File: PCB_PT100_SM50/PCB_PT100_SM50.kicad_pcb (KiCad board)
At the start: 2 copper layers, 80 x 65 mm, 62 parts, among them U1 TPD4E1U06DBVR, U2 INA826AIDR, U3 TPS7A4901DGNT, U4 INA826AIDR, U5 OPA2188AIDR, U6 REF3012AIDBZR, U7 TPD4E1U06DBVR, U8 78L05 5V

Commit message: Publish final PCB project
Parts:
- added C24: 100nF, Capacitor_SMD:C_0805_2012Metric, F.Cu at (27.9, 41.2)
- added C25: 10uF, Capacitor_SMD:C_0805_2012Metric, F.Cu at (34.9, 41.1)
- added C26: 0.1uF, Capacitor_SMD:C_0805_2012Metric, F.Cu at (30.9, 42.1)
- added G***: LOGO, Images:logoucr, F.Cu at (64.3, 20.2)
- added REF**: KiCad-Logo2_5mm_SilkScreen, Symbol:KiCad-Logo2_5mm_SilkScreen, F.Cu at (81.9, 42.2)
- J_PT100_1: footprint TerminalBlock_Phoenix:TerminalBlock_Phoenix_MKDS-1,5-3_1x03_P5.00mm_Horizontal -> ProyectoPCB:CONN_AST0250304_MZC
- J_SM50: footprint TerminalBlock_Phoenix:TerminalBlock_Phoenix_MKDS-1,5-4_1x04_P5.00mm_Horizontal -> ProyectoPCB:AST0250404
- U3: footprint Package_SO:MSOP-8-1EP_3x3mm_P0.65mm_EP1.73x1.85mm -> ProyectoPCB_Footprints:TPS7A4901DGNT_DGN8_1P89X1P57
- moved C13 44.3 mm to (76.9, 71.1), turned to 0 degrees
- moved C17 41.7 mm to (56.9, 42.2), turned to -90 degrees
- moved C15 40.9 mm to (58.9, 42.0), turned to -90 degrees
- moved C16 40.8 mm to (62.9, 50.1)
- moved C11 40.7 mm to (76.9, 69.1), turned to 0 degrees
- moved C18 39.0 mm to (64.9, 50.0)
- moved U6 36.9 mm to (29.9, 46.1)
- moved F6 29.7 mm to (64.1, 45.2), turned to 180 degrees
- moved C22 29.4 mm to (25.9, 44.2), turned to 180 degrees
- moved C20 29.2 mm to (49.1, 63.2), turned to 0 degrees
- moved R2 28.4 mm to (30.8, 31.2)
- moved F4 26.4 mm to (71.1, 73.1), turned to 180 degrees
- moved F5 25.9 mm to (63.7, 40.2), turned to 180 degrees
- moved C10 24.0 mm to (52.0, 27.2), turned to 0 degrees
- moved C2 23.1 mm to (33.6, 30.2), turned to 90 degrees
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- renumbered C_OUT_SM50 to C27, C_OUT_PT100 to C28, R_LIM_SM50 to R11, R_ISO_PT100 to R12, R_ISO_SM50 to R13, RSET_PT100 to R14, R_LIM_PT100 to R9, TRIM_SM50 to RV1, TRIM_PT100 to RV2
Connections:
- H1 pad 1: (no net) -> GND
- H2 pad 2: (no net) -> GND
- H3 pad 3: (no net) -> GND
- H4 pad 4: (no net) -> GND
- J_BBOX_PT100 pad 3: Net-(J_BBOX_PT100-GND_3) -> GND
- J_BBOX_PT100 pad 6: Net-(J_BBOX_PT100-GND_3) -> GND
- J_BBOX_SM50 pad 3: Net-(J_BBOX_SM50-GND_3) -> GND
- J_BBOX_SM50 pad 6: Net-(J_BBOX_SM50-GND_3) -> GND
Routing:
- net /+15V_PROT_PT100: track 0.00 -> 81.3 mm
- net /+15V_PROT_SM50: track 0.00 -> 55.4 mm
- net /-15V_PROT_PT100: track 0.00 -> 54.0 mm
- net /PT100_1_RETURN: track 0.00 -> 51.9 mm
- net /PT100_1_SENSE: track 0.00 -> 46.6 mm
- net /PT100_1_FORCE: track 0.00 -> 38.4 mm
- net /+5V_REF: track 0.00 -> 35.3 mm
- net /-15V_PROT_SM50: track 0.00 -> 32.1 mm
- net /-15V_BBOX_SM50: track 0.00 -> 28.0 mm
- net /-15V_BBOX_PT100: track 0.00 -> 27.2 mm
- net /+10V_SM50: track 0.00 -> 24.9 mm
- net /PT100_OUT_P: track 0.00 -> 22.1 mm
- net /SM50_SIG_P: track 0.00 -> 20.8 mm
- net /SM50_SIG_N: track 0.00 -> 18.2 mm
- net Net-(U4--IN): track 0.00 -> 17.1 mm
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- added copper zone on B.Cu, net GND
- added copper zone on F.Cu, net GND
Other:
- outline, holes or cut-outs redrawn
- board text added: "Acondicionamiento de Señales"
- board text added: "C15"
- board text added: "KDVJ C09331 PCB v0"
- board text added: "Sensores: PT100 Y SM-50"

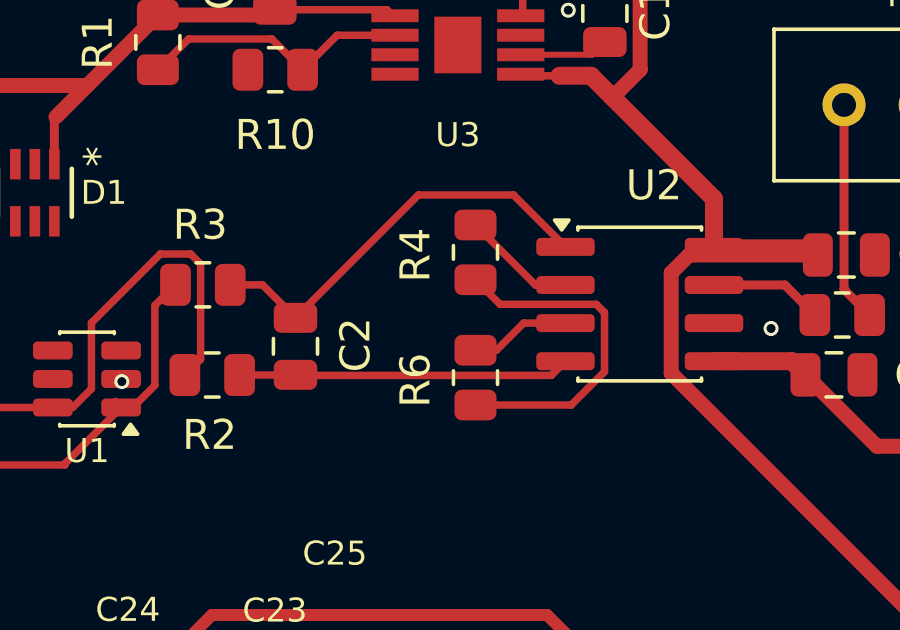
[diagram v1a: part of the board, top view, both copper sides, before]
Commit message: Update LTspice schematics and fabrication outputs
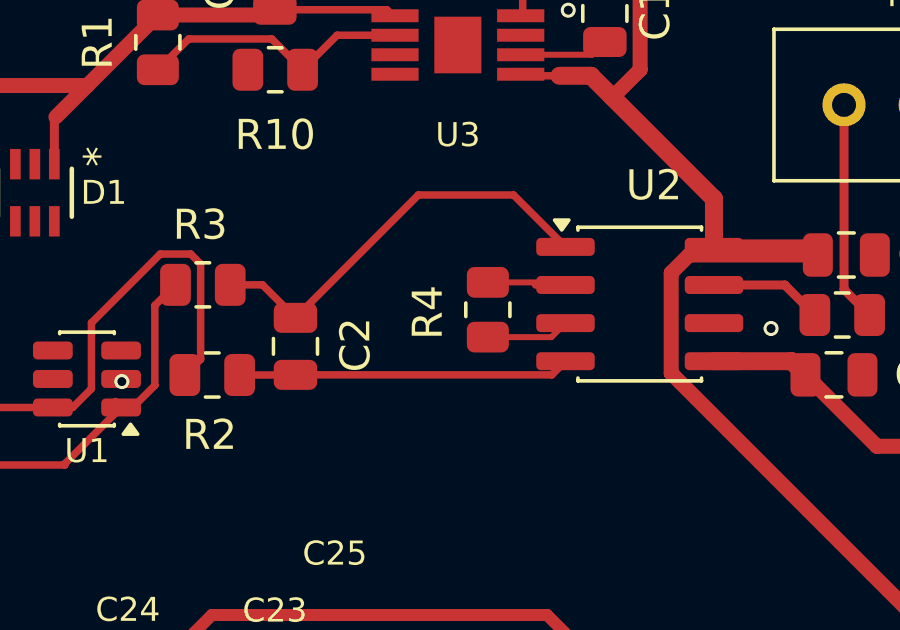
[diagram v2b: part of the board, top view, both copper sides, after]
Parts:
- removed R6: 180, Resistor_SMD:R_0805_2012Metric
- moved R4 1.96 mm to (40.0, 29.0)
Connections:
- U2 pad 3: Net-(R6-Pad2) -> Net-(R4-Pad2)
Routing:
- net Net-(R4-Pad2): track 11.7 -> 2.78 mm
- net Net-(R6-Pad2): track 3.37 -> 0.00 mm

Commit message: Restaurar version SM-50 0-5V
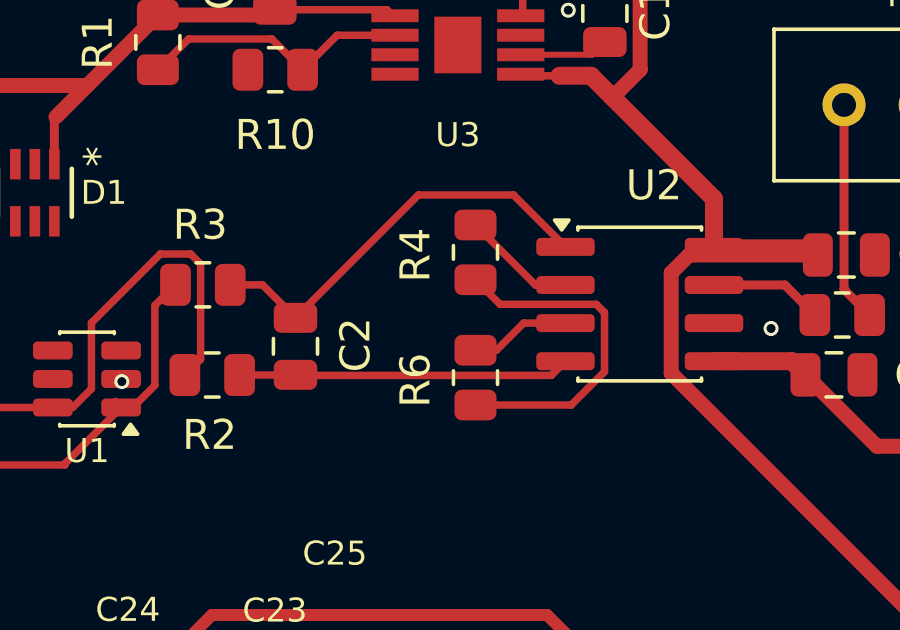
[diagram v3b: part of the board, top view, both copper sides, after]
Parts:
- added R6: 180, Resistor_SMD:R_0805_2012Metric, F.Cu at (39.6, 31.3)
- moved R4 1.96 mm to (39.6, 27.1)
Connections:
- U2 pad 3: Net-(R4-Pad2) -> Net-(R6-Pad2)
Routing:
- net Net-(R4-Pad2): track 2.78 -> 11.7 mm
- net Net-(R6-Pad2): track 0.00 -> 3.37 mm
